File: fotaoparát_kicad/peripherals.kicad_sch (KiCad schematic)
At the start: 27 parts, among them J13 Micro_SD_Card_Det2, J4 BUTTONS

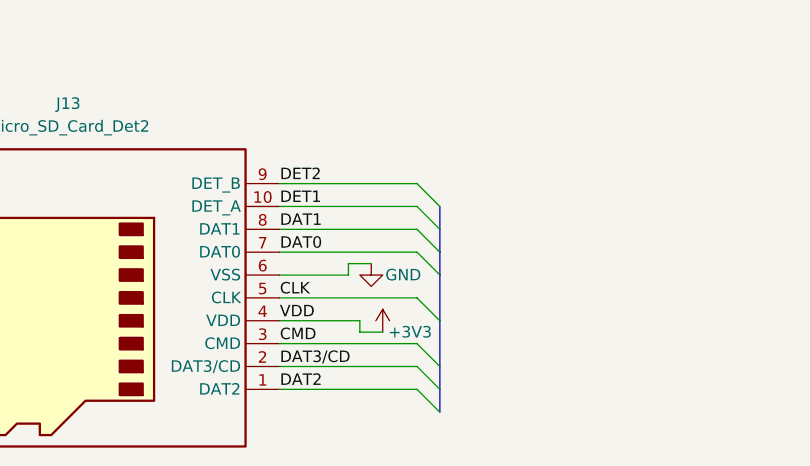
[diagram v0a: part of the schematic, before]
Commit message: Udelal jsem: -Predelani labelu na global -Pridani vyvodu na desku pro spoust -Pokusil se predelat ten stepdown, Vout by mela byt 1V1, nestihl jsem prepsat vsechny hodnoty a pridat lscs cisla
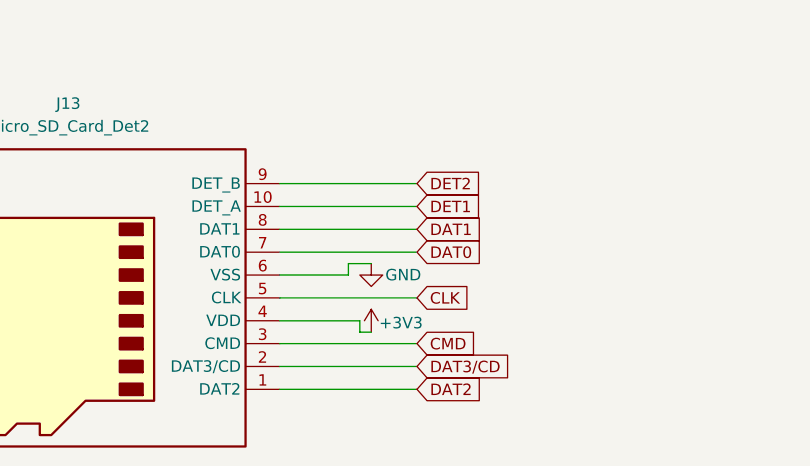
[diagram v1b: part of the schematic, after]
